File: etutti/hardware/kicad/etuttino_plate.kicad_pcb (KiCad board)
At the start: 2 copper layers, 183.4 x 88.2 mm, 8 parts

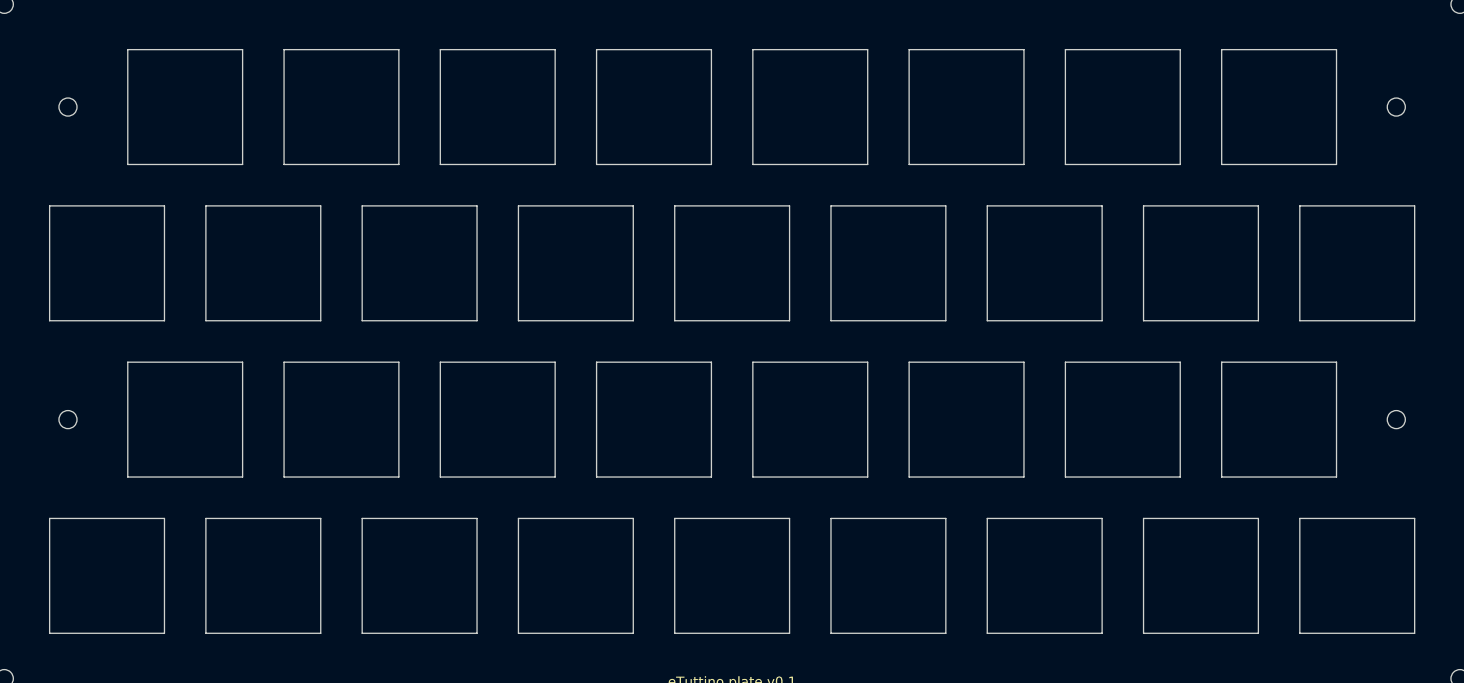
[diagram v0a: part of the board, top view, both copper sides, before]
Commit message: eTuttino: round keys, row 1 at the bottom, B-griff, presets, keyboard toggle
Page:
- Round accordion buttons (on-screen and in the model renders).
- Row 1 is now nearest the player (bottom), row 4 at the top.
- C-griff / B-griff switch (B = mirror image, rows 1 and 3 swapped);
  sent to the Teensy as CC 24 so the physical keys follow. Remembered.
- Computer-keyboard input is now a toggle (remembered) with the new
  mapping: row 1 Z..Comma, row 2 A..L, row 3 W..O, row 4 2..0 (by
  physical key, so it matches ABNT2). Key legends hide when it's off.
- Synth: instrument presets (classic accordion = default = two reeds a
  few cents apart in a soft cassotto; jazz accordion; piano; bass;
  guitar), "Reset to default", a "modified" marker, and voice 2
  controls (waveform, octave, level, detune).

Firmware: two oscillators per voice (voice 2 waveform/level/detune/
octave on CC 20-23), C/B-griff note tables switchable by CC 24 (held
keys release the note they started), row pins reordered for the flipped
PCB, defaults = the classic accordion preset. Compiled clean
(teensy40, usb=midi) and uploaded to the connected Teensy.

PCB: flipped so row 1 is at the front; router now ranks rows/columns by
height instead of row number; still DRC-clean. build_pcb.py now reads
the board back and checks every key's row/column pins against the
firmware tables (fails on mismatch; mutation-tested).

Co-Authored-By: Claude Opus 5.5 <noreply@anthropic.com>
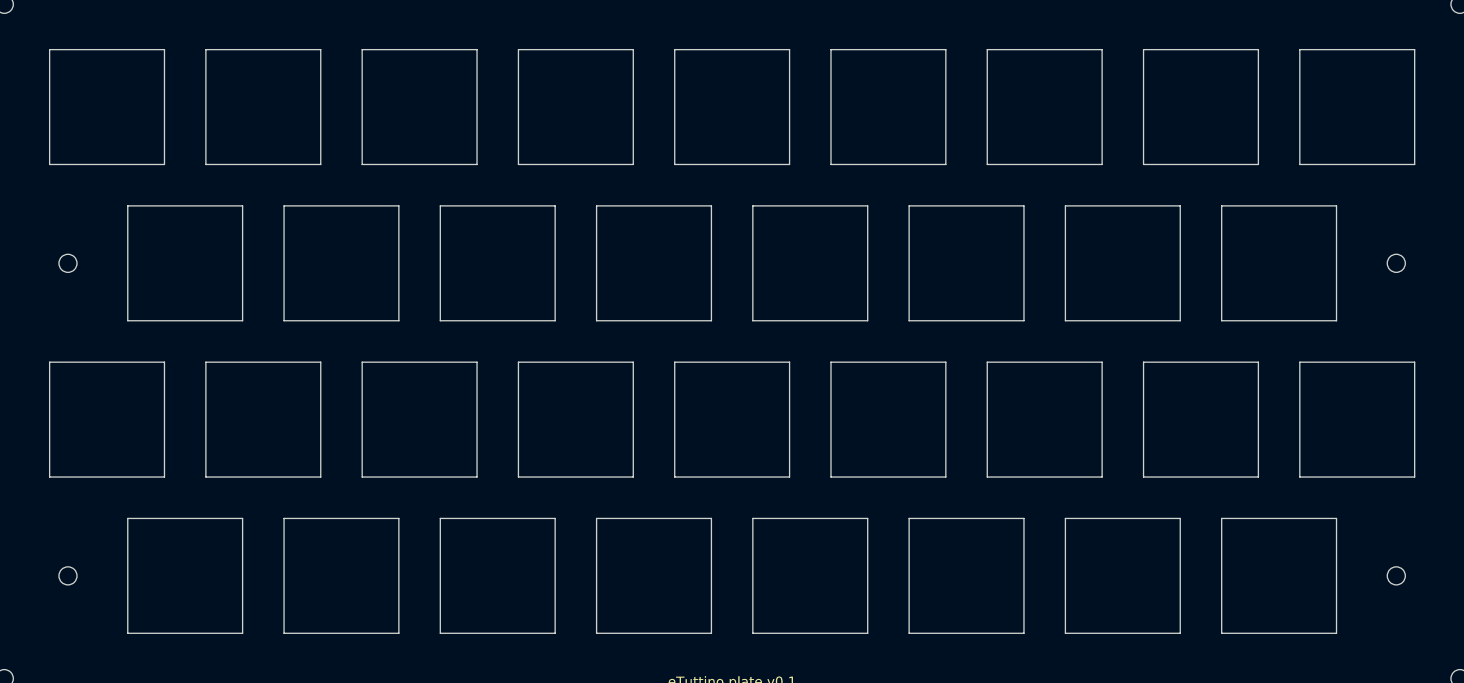
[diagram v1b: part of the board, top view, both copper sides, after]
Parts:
- moved H7 57.1 mm to (10.8, 116.7)
- moved H8 57.1 mm to (172.7, 116.7)
- moved H10 19.0 mm to (172.7, 78.6)
- moved H9 19.0 mm to (10.8, 78.6)
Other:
- outline, holes or cut-outs redrawn

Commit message: eTuttino: Hall-effect keys with velocity, assembly and user manuals
PCB (etutti/hardware):
- Gateron magnetic switches (no pins, plate mounted) with a DRV5056A3
  Hall sensor under each one, on the BACK of a 1.2 mm board: the DRV5056
  only reads a south pole facing its marked side and Gateron magnets are
  north-down, so the field has to come through the board from behind.
- 3 x CD74HC4067 analog muxes (address on pins 0-3, outputs to A0-A2),
  AMS1117-3.3 rail from VIN for the 34 sensors (~200 mA).
- build_pcb.py: fixed per-key wiring and power buses, then its own A*
  grid router (two layers, vias, KiCad clearances) for everything else.
  DRC 0/0/0, firmware cross-check 34/34. JLCPCB BOM/CPL for bottom-side
  assembly. generate.py owns the sensor -> mux channel map and prints the
  firmware's KEY_INPUT table.

Firmware: reads the sensors through the muxes (~240 us per full scan,
measured), cube-root travel model between per-key rest and learnt bottom
(EEPROM), velocity from the time between 12 % and 45 % of the travel.
CC 9 velocity curve, CC 14 recalibrate, CC 15 key-test stream. Pull-downs
on the mux outputs: a bare Teensy has no stray notes (verified on the
user's Teensy: 0 keys present, 0 notes).

Page: "eTuttino keys" panel (velocity curve, Calibrate, Key test rings),
link to the new etutti/manuais/ page: assembly route A (factory-soldered
via JLCPCB PCBA), route B (soldered at home), final assembly, user manual,
in en/pt/es.

Co-Authored-By: Claude Opus 5.5 <noreply@anthropic.com>
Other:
- board text added: "eTuttino plate v0.2"
- board text removed: "eTuttino plate v0.1"

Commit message: eTuttino: Castagnari Magica K2 layout, slim board, browser sound, manual visuals
- Layout: 41 keys like the Castagnari Magica K2 treble keyboard (rows
  A3..D#6, G3..G6, G#3..D6, A3..C5), on the page, in the firmware and on
  the board; computer-keyboard mapping extended (ABNT2), legends from
  navigator.keyboard.getLayoutMap() where available.
- Board 267 x 88.2 mm, only the four key rows tall: the Teensy + Audio
  Board stack sits in the corner row 4 leaves free (USB and headphone
  jack at the right edge), Audio Board soldered low so the stack (~17 mm)
  stays below the keycaps (~19 mm); plate notched; muxes behind row 4.
  Router: power buses joined by the router, critical nets before the
  sensor outputs, retry with the failed net first, layer changes next to
  an existing via reuse it. DRC 0/0/0, firmware cross-check 41/41.
- "Listen in this browser" (websynth.js): the eTuttino's sounds through
  the computer's speakers, off until the user switches it on; same CCs
  as the firmware.
- Manuals rewritten for the new board in en/pt/es, with 3D renders
  (assembly3d.py: simple VRML switches, keycaps, plate, Teensy, Audio
  Board) and close-ups; click opens the full-resolution image.

Co-Authored-By: Claude Opus 5.5 <noreply@anthropic.com>
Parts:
- added H1: MountingHole_2.2mm_M2, MountingHole_2.2mm_M2, F.Cu at (3.00, 3.00)
- added H2: MountingHole_2.2mm_M2, MountingHole_2.2mm_M2, F.Cu at (3.00, 85.2)
- moved H5 257.4 mm to (256.6, 85.2)
- moved H3 224.0 mm to (222.7, 3.00)
- moved H6 178.9 mm to (10.8, 72.7)
- moved H9 139.0 mm to (134.6, 15.5)
- moved H7 82.1 mm to (10.8, 34.6)
- moved H10 77.7 mm to (218.2, 15.5)
- moved H4 76.2 mm to (256.6, 47.1)
- moved H8 76.0 mm to (234.6, 72.7)
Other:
- board size 183.4 x 88.2 mm -> 259.6 x 88.2 mm
- board text added: "eTuttino plate v0.3"
- board text removed: "eTuttino plate v0.2"

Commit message: eTuttino: 44-key layout, power LED, muxes spread out, no brand reference
- Row 2 now ends at E6 (12 keys); row 4 runs A3..C6 (10 keys) on row 2's
  columns (A3 above A#3, C6 above C#6); row 1 unchanged.
- Bicolour power LED D1 (pins 4/5 via R1/R2 330R): orange while the keys
  are first read, green playing, red blinking on codec/sensor errors.
- Multiplexers: U51 front-right corner, U53 back-left corner, U52 beside
  the Teensy. The router picks each sensor's mux channel and writes
  KEY_INPUT into the sketch; the far mux's long lines route last.
- High-note reed tables in the firmware (the full tables aliased).
- Board DRC 0/0/0, firmware cross-check 44/44; renders and manuals
  (en/pt/es) updated, incl. a U53 close-up.
- Removed every mention of the commercial accordion layout reference.

Co-Authored-By: Claude Opus 5.5 <noreply@anthropic.com>
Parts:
- removed H10: MountingHole_2.2mm_M2, MountingHole_2.2mm_M2
- moved H9 86.0 mm to (220.6, 15.5)
- moved H4 19.1 mm to (237.6, 48.0)
- moved H5 19.0 mm to (237.6, 85.2)
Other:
- board size 259.6 x 88.2 mm -> 240.6 x 88.2 mm
- board text added: "eTuttino plate v0.4"
- board text removed: "eTuttino plate v0.3"

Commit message: eTuttino: Teensy stack on the left, 3D-printed case, stiffer board
- Ergonomic layout: the Teensy + Audio Board sit in the back-left corner,
  USB and headphone jack facing the left edge (cables away from the
  playing hand). Muxes, LDO and holes follow; the power LED sits just in
  front of the stack, U52 in a new 15 mm back strip. 267 x 97.2 mm,
  rerouted: DRC 0/0/0, firmware check 44/44 (KEY_INPUT updated, flashed).
- Case: case.py (FreeCAD) builds a tray + top shell (STL/STEP in fab/):
  stepped key opening, LED window, pod over the stack with USB/jack
  openings. case_check.py proves it touches no keycap over its travel,
  no switch and nothing of the stack.
- Stiffness: mechanics.py puts 43 pillars in the tray where the back of
  the board has only traces, and estimates the sag under a 3 N press
  (2.6 mm on the mounting holes alone, 0.027 mm in the case).
- Renders: all 28 stacking-header legs through the board with solder,
  the Teensy's pin spacers and tips, switch bases on the board, the
  finished case, the tray. Manuals (en/pt/es) and README updated, with
  where to get the case printed.

Co-Authored-By: Claude Opus 5.5 <noreply@anthropic.com>
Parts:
- moved H1 261.2 mm to (264.0, 12.0)
- moved H2 261.2 mm to (264.0, 94.2)
- moved H6 245.6 mm to (256.2, 81.7)
- moved H7 245.6 mm to (256.2, 43.6)
- moved H4 208.4 mm to (29.4, 57.0)
- moved H5 208.4 mm to (29.4, 94.2)
- moved H8 202.4 mm to (32.4, 81.7)
- moved H3 178.6 mm to (44.3, 12.0)
- moved H9 174.5 mm to (46.4, 24.5)
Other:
- outline, holes or cut-outs redrawn
- board text added: "eTuttino plate v0.5"
- board text removed: "eTuttino plate v0.4"

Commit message: eTuttino board v0.6 for the v7 case: hex grid 18.5, case outline, J3
- generate.py reads case/out/pcb_envelope.json: keys on the 18.5 mm
  hexagonal grid (rows 16.02 apart), the board outline (case cavity - 0.5,
  notched round the screw bosses), the bottom-plate pillars, the stack
  position from fit_check.py; ROWS, notes and firmware semantics unchanged
- build_pcb.py routes inside the outline polygon; the power LED moved to
  the controls board: R1/R2 stay, J3 (JST PH 8) carries 3.3 V, GND, pot
  (22), encoder A/B/SW (17/9/6), LED R/G; fails if a back-side part sits
  on a pillar; route order OUT_U41,OUT_U42,GND,LED_R,LED_G_DRV,OUT_U34
- result: DRC 0 errors / 0 warnings / 0 unconnected, firmware 44/44;
  KEY_INPUT rewritten in the sketch (compiles)
- case: pillar_points had rows 2-3 wrong (5.3 mm from a sensor); now one
  per three-key triangle (64): worst sag 0.044 mm at 3 N (was 0.37);
  envelope outlines now notched; FIT_CHECK lists what the board asks of
  the case
- mechanics.py checks the v7 board on those pillars; the #78 FreeCAD case
  (case.py, case_check.py, fab/etuttino_case_*) is removed; --renders off
  until the manuals are redone

Co-Authored-By: Claude Opus 5.5 <noreply@anthropic.com>
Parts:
- removed H1, H2, H3, H4, H5, H6, H7, H8, H9: MountingHole_2.2mm_M2, MountingHole_2.2mm_M2
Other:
- board size 240.6 x 88.2 mm -> 254.4 x 85.4 mm
- board text added: "eTuttino plate v0.6"
- board text removed: "eTuttino plate v0.5"

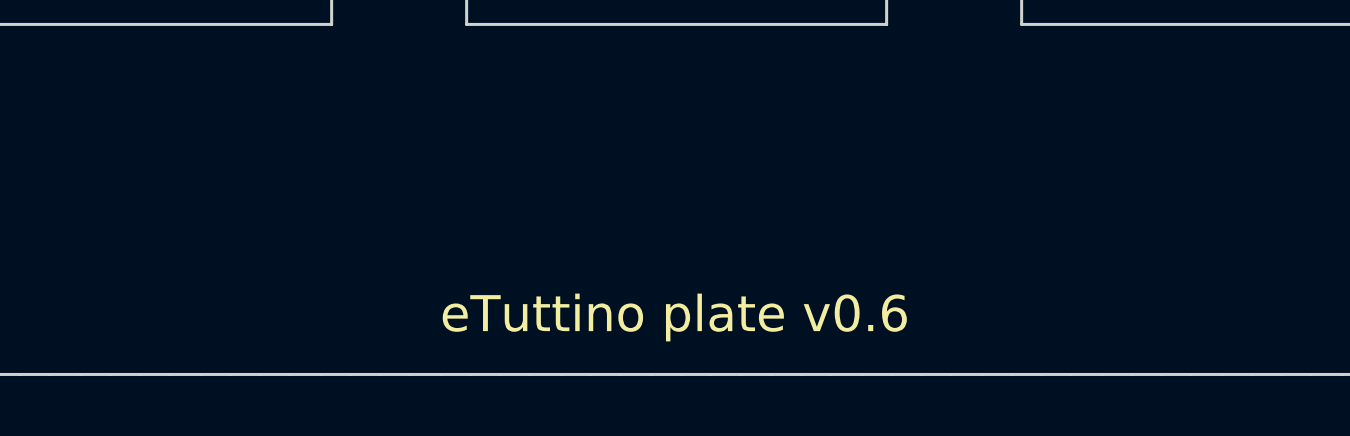
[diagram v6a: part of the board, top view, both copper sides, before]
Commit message: eTuttino v8: M2 board screws, 1.6 mm plate, controls board, firmware knobs
Implements case SPEC v8 (PR #88):
- case: 1.6 mm FR-4 plate (key tops z 26.6); two M2 screws from below
  through thicker pillars (30;60) and (12;70) with counterbores; two
  posts under the interface lid for the controls board; exports both in
  the PCB envelope
- main board v0.7: holes H1/H2 with a 3.5 mm copper-free ring, plate
  Gerbers at 1.6 mm; DRC 0/0/0, firmware 44/44, KEY_INPUT unchanged
- controls_pcb.py: the controls board (RK09K volume pot, EC11E encoder
  with switch, 3 mm red/green LED, vertical JST PH facing down to J3),
  routed with build_pcb's router; DRC 0/0/0
- firmware: pot (22) sets the volume and sends CC 7 back, ignored when no
  pot is detected at boot (checked on the real Teensy); encoder (17/9)
  steps the instrument and sends CC 25; its button confirms (saved to
  EEPROM) or returns to the default sound; LED blinks green while pending
- fit_check: the real controls board, its JST and cable, the M2 nuts;
  the side-entry JST hit the Chorus speaker, so it is a vertical one now

Co-Authored-By: Claude Opus 5.5 <noreply@anthropic.com>
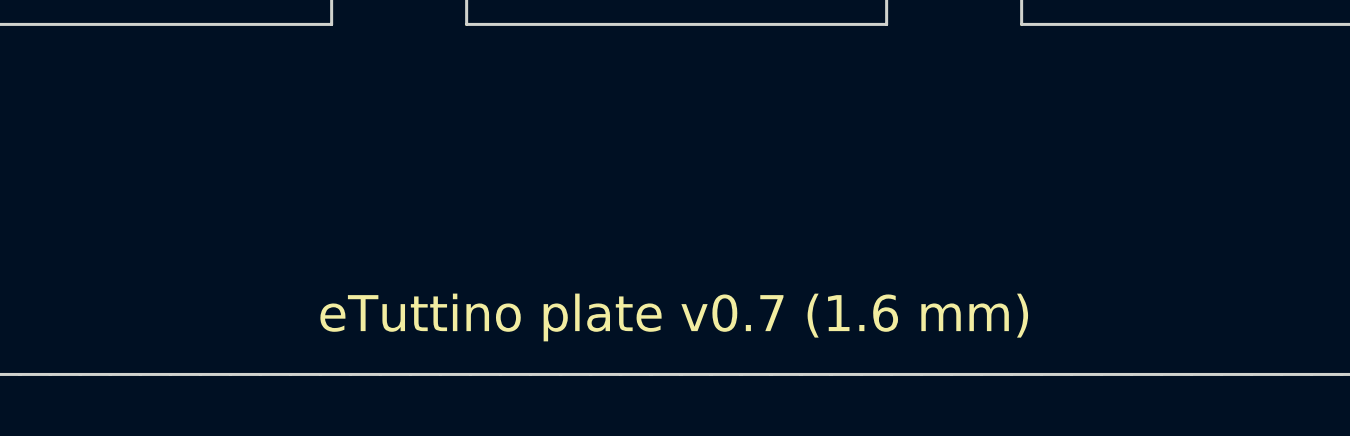
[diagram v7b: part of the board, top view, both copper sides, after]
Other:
- board text added: "eTuttino plate v0.7 (1.6 mm)"
- board text removed: "eTuttino plate v0.6"
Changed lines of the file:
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@@
 		(layer "Edge.Cuts")
 	)
-	(gr_text "eTuttino plate v0.6"
+	(gr_text "eTuttino plate v0.7 (1.6 mm)"
 		(at 196.445499 90.7 0)
 		(layer "F.SilkS")
